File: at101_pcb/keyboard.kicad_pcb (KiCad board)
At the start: 2 copper layers, 443.7 x 141.9 mm, 247 parts, among them SW1.1 KEY_ESCAPE, SW1.10 KEY_F9, SW1.11 KEY_F10, SW1.12 KEY_F11, SW1.13 KEY_F12, SW1.14 KEY_PRINTSCREEN, SW1.15 KEY_SCROLL_LOCK, SW1.16 KEY_PAUSE, SW1.2 KEY_F1, SW1.3 KEY_F2, SW1.4 KEY_F3, SW1.5 KEY_F4, SW1.6 KEY_F5, SW1.7 KEY_F6, SW1.8 KEY_F7, SW1.9 KEY_F8, SW2.1 KEY_BACKQUOTE, SW2.10 KEY_9, SW2.11 KEY_0, SW2.12 KEY_MINUS, SW2.13 KEY_EQUALS, SW2.14 KEY_BACKSPACE, SW2.15 KEY_INSERT, SW2.16 KEY_HOME, SW2.17 KEY_PGUP, SW2.18 KEY_NUMLOCK, SW2.19 KEY_NUMDIVIDE, SW2.2 KEY_1, SW2.20 KEY_NUMTIMES, SW2.21 KEY_NUMMINUS, SW2.3 KEY_2, SW2.4 KEY_3, SW2.5 KEY_4, SW2.6 KEY_5, SW2.7 KEY_6, SW2.8 KEY_7, SW2.9 KEY_8, SW3.1 KEY_TAB, SW3.10 KEY_O, SW3.11 KEY_P, SW3.12 KEY_LEFTBRACKET, SW3.13 KEY_RIGHTBRACKET, SW3.14 KEY_ANSIBACKSLASH, SW3.15 KEY_DELETE, SW3.16 KEY_END, SW3.17 KEY_PGDN, SW3.18 KEY_NUM7, SW3.19 KEY_NUM8, SW3.2 KEY_Q, SW3.20 KEY_NUM9, SW3.21 KEY_NUMPLUS, SW3.3 KEY_W, SW3.4 KEY_E, SW3.5 KEY_R, SW3.6 KEY_T, SW3.7 KEY_Y, SW3.8 KEY_U, SW3.9 KEY_I, SW3B.1 KEY_NUMBIGPLUS, SW4.1 KEY_CAPSLOCK, SW4.10 KEY_L, SW4.11 KEY_SEMICOLON, SW4.12 KEY_QUOTE, SW4.13 KEY_ISOBACKSLASH, SW4.14 KEY_ISOENTER, SW4.15 KEY_ENTER, SW4.16 KEY_NUM4, SW4.17 KEY_NUM5, SW4.18 KEY_NUM6, SW4.19 KEY_NUMEQUALS, SW4.2 KEY_A, SW4.3 KEY_S, SW4.4 KEY_D, SW4.5 KEY_F, SW4.6 KEY_G, SW4.7 KEY_H, SW4.8 KEY_J, SW4.9 KEY_K, SW4.B1 KEY_CAPSLOCK_1.5, SW4C.1 KEY_CAPSLOCK_1.25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

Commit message: Correct AT10[12]W? switch labels
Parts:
- removed the D1 at (507.3, 65.5)
- added D2: CAPS_LOCK_LED, LED_THT:LED_Rectangular_W5.0mm_H2.0mm, F.Cu at (504.8, 65.5)
- renumbered D2 to D1, R2 to R1, R3 to R2, R1 to R3, SW3B.1 to SW3B.21, SW4.15 to SW4.14, SW4.16 to SW4.15, SW4.17 to SW4.16, SW4.18 to SW4.17, SW4.19 to SW4.18, SW4.14 to SW4.B14, SW6.9 to SW6.10, SW6.10 to SW6.11, SW6.11 to SW6.12, SW6.12 to SW6.13, SW6B.13 to SW6.7, SW6.7 to SW6.8, SW6.8 to SW6.9, SW6B.7 to SW6B.8
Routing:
- net COL9: track 692.2 -> 625.3 mm
- net ROW2: track 289.8 -> 291.9 mm
- net Net-(D4.14-Pad2): track 21.2 -> 23.0 mm
- net CAPS_LOCK_LED: track 7.66 -> 9.26 mm
- net COL10: track 610.0 -> 609.0 mm
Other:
- board text added: "AT10[12]W? PCB Henrik O. Sørensen Rev 1.03"
- board text removed: "AT10[12]W? PCB Henrik O. Sørensen Rev 1.0"

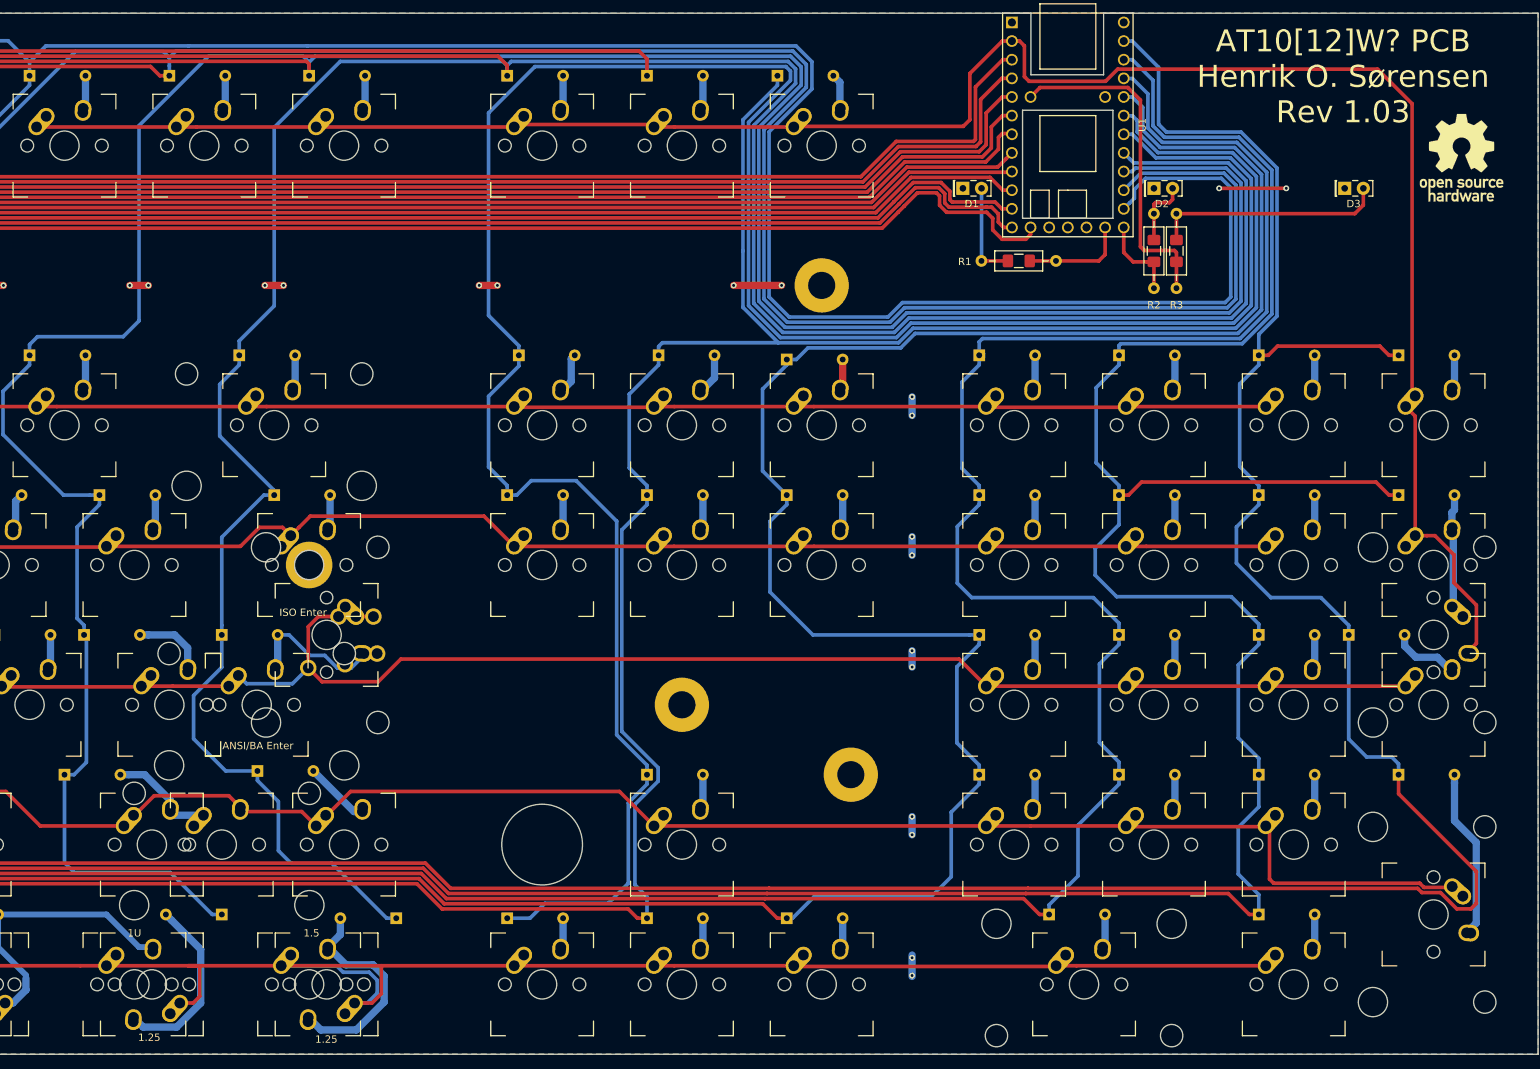
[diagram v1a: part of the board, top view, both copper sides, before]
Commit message: Correct nav and numeric cluster distances
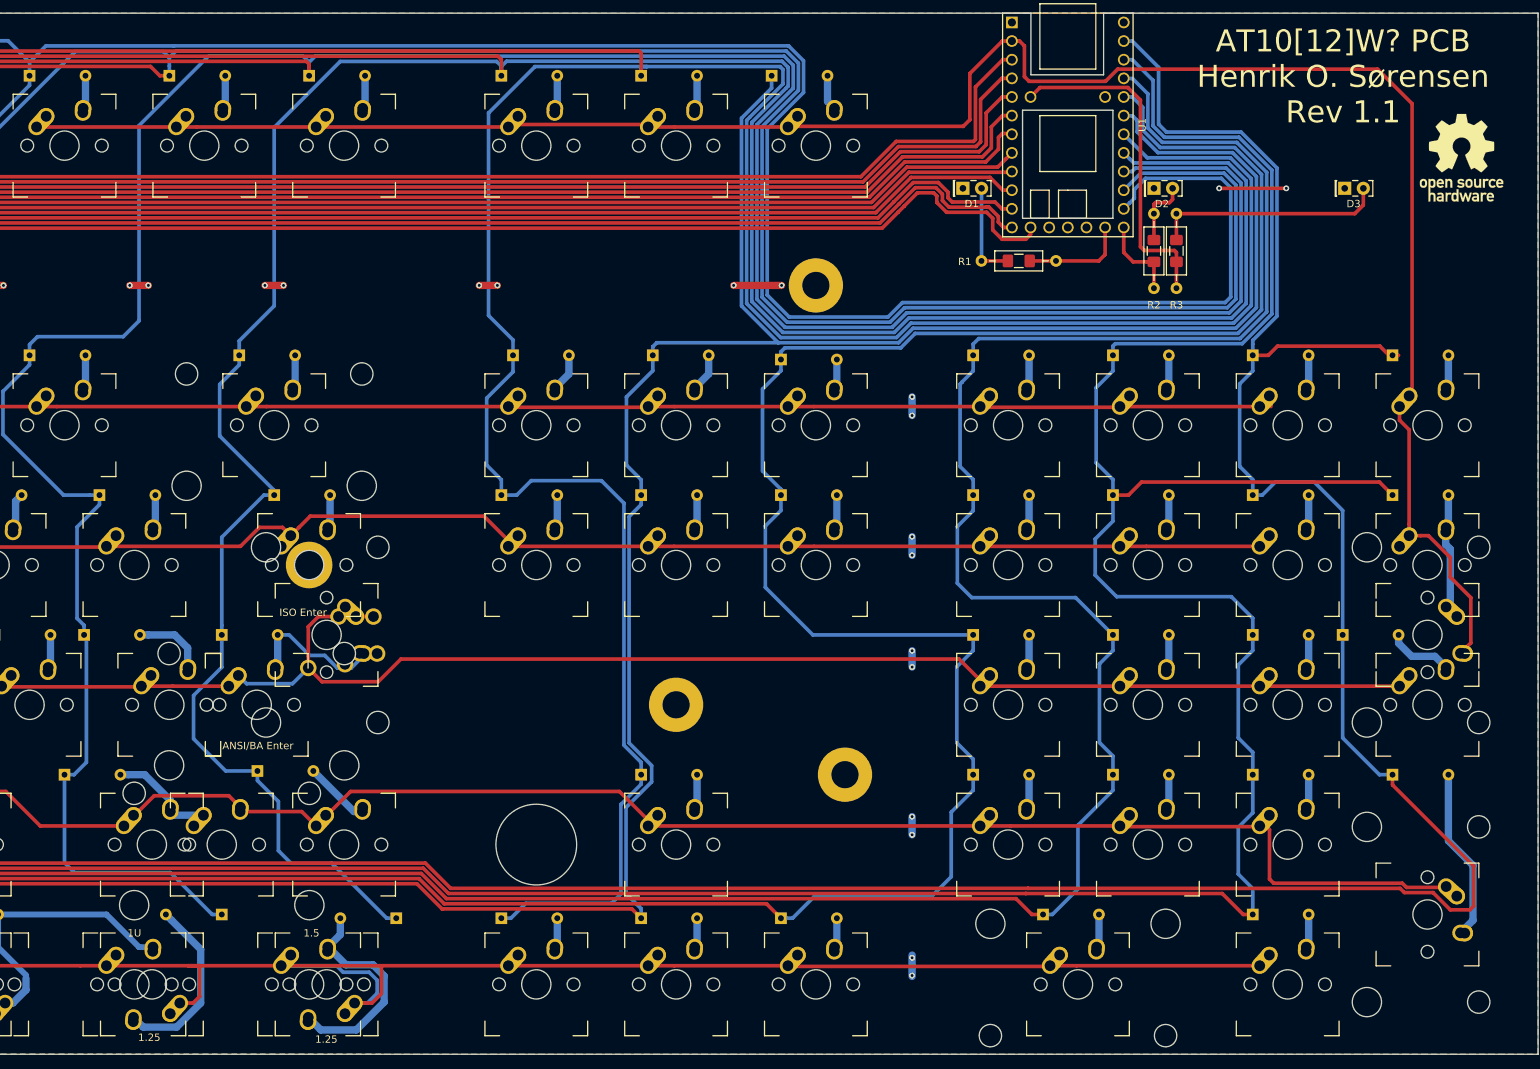
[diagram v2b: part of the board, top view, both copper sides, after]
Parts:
- moved D2.21 0.83 mm to (537.3, 88.3)
- moved D3.21 0.83 mm to (537.3, 107.3)
- moved D4.18 0.83 mm to (530.5, 126.4)
- moved D5.19 0.83 mm to (537.3, 145.4)
- moved D6.12 0.83 mm to (489.7, 164.5)
- moved SW2.20 0.83 mm to (523.0, 97.8)
- moved SW3.20 0.83 mm to (523.0, 116.8)
- moved SW4.17 0.83 mm to (523.0, 135.9)
- moved SW5.18 0.83 mm to (523.0, 154.9)
- moved SW6.12 0.83 mm to (494.5, 174.0)
- moved SW6.13 0.83 mm to (523.0, 174.0)
- moved D2.18 0.83 mm to (480.2, 88.3)
- moved D2.19 0.83 mm to (499.2, 88.3)
- moved D3.18 0.83 mm to (480.2, 107.3)
- moved D3.19 0.83 mm to (499.2, 107.3)
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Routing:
- net COL8: track 596.4 -> 592.5 mm
- net COL9: track 625.3 -> 622.5 mm
- net COL6: track 647.0 -> 645.3 mm
- net COL5: track 686.1 -> 687.9 mm
- net COL1: track 972.5 -> 971.1 mm
- net COL2: track 770.2 -> 769.0 mm
- net COL3: track 748.5 -> 747.3 mm
- net Net-(D2.15-Pad2): track 6.28 -> 5.23 mm
- net ROW10: track 524.5 -> 523.9 mm
- net Net-(D6.12-Pad2): track 5.17 -> 4.58 mm
- net Net-(D1.15-Pad2): track 5.17 -> 4.58 mm
- net Net-(D5.15-Pad2): track 5.17 -> 4.58 mm
- net Net-(D6.9-Pad2): track 4.67 -> 4.07 mm
- net Net-(D6.13-Pad2): track 5.17 -> 4.58 mm
- net Net-(D2.16-Pad2): track 5.83 -> 5.23 mm
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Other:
- board text added: "AT10[12]W? PCB Henrik O. Sørensen Rev 1.1"
- board text removed: "AT10[12]W? PCB Henrik O. Sørensen Rev 1.03"
